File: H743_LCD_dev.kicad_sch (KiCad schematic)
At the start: 4 parts

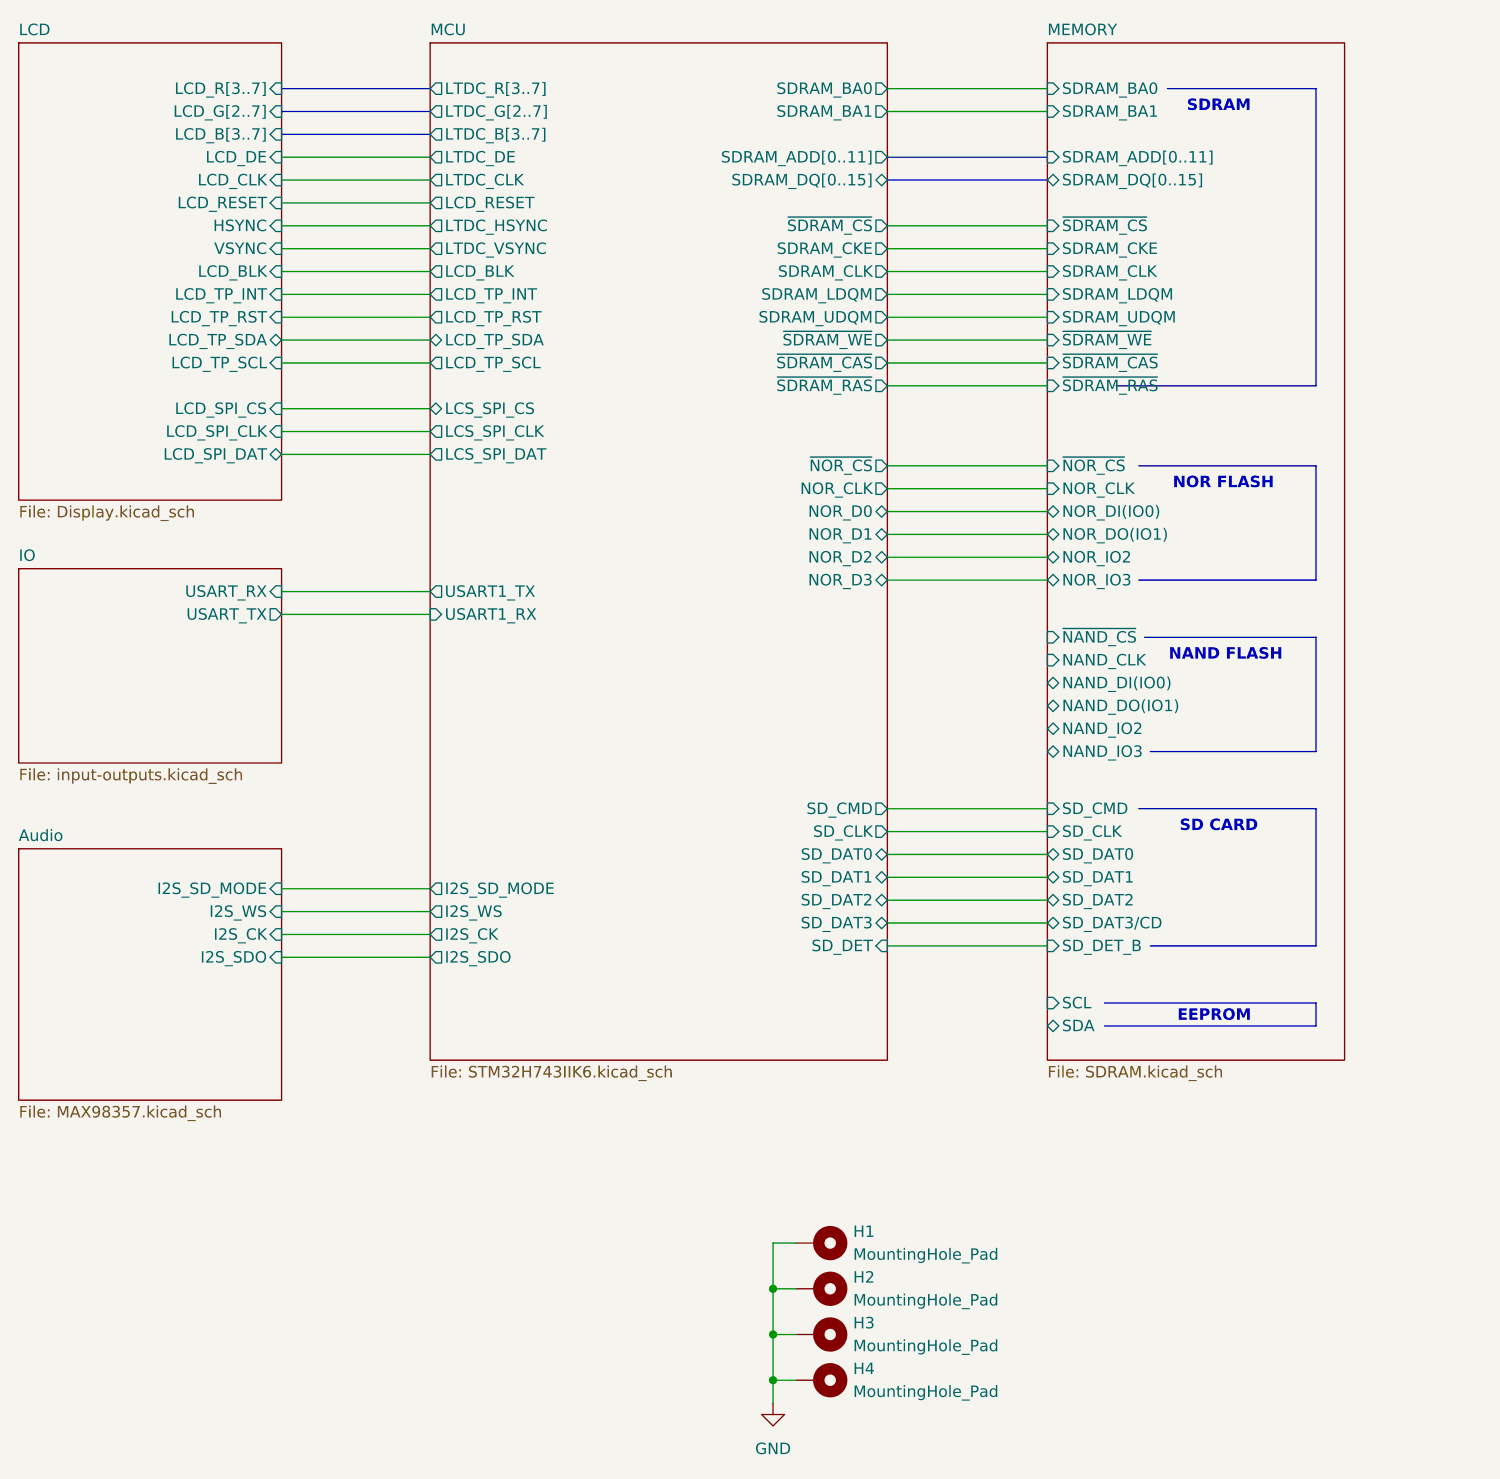
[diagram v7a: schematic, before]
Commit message: All clear (need to verify). LCD backlight driver left untracked
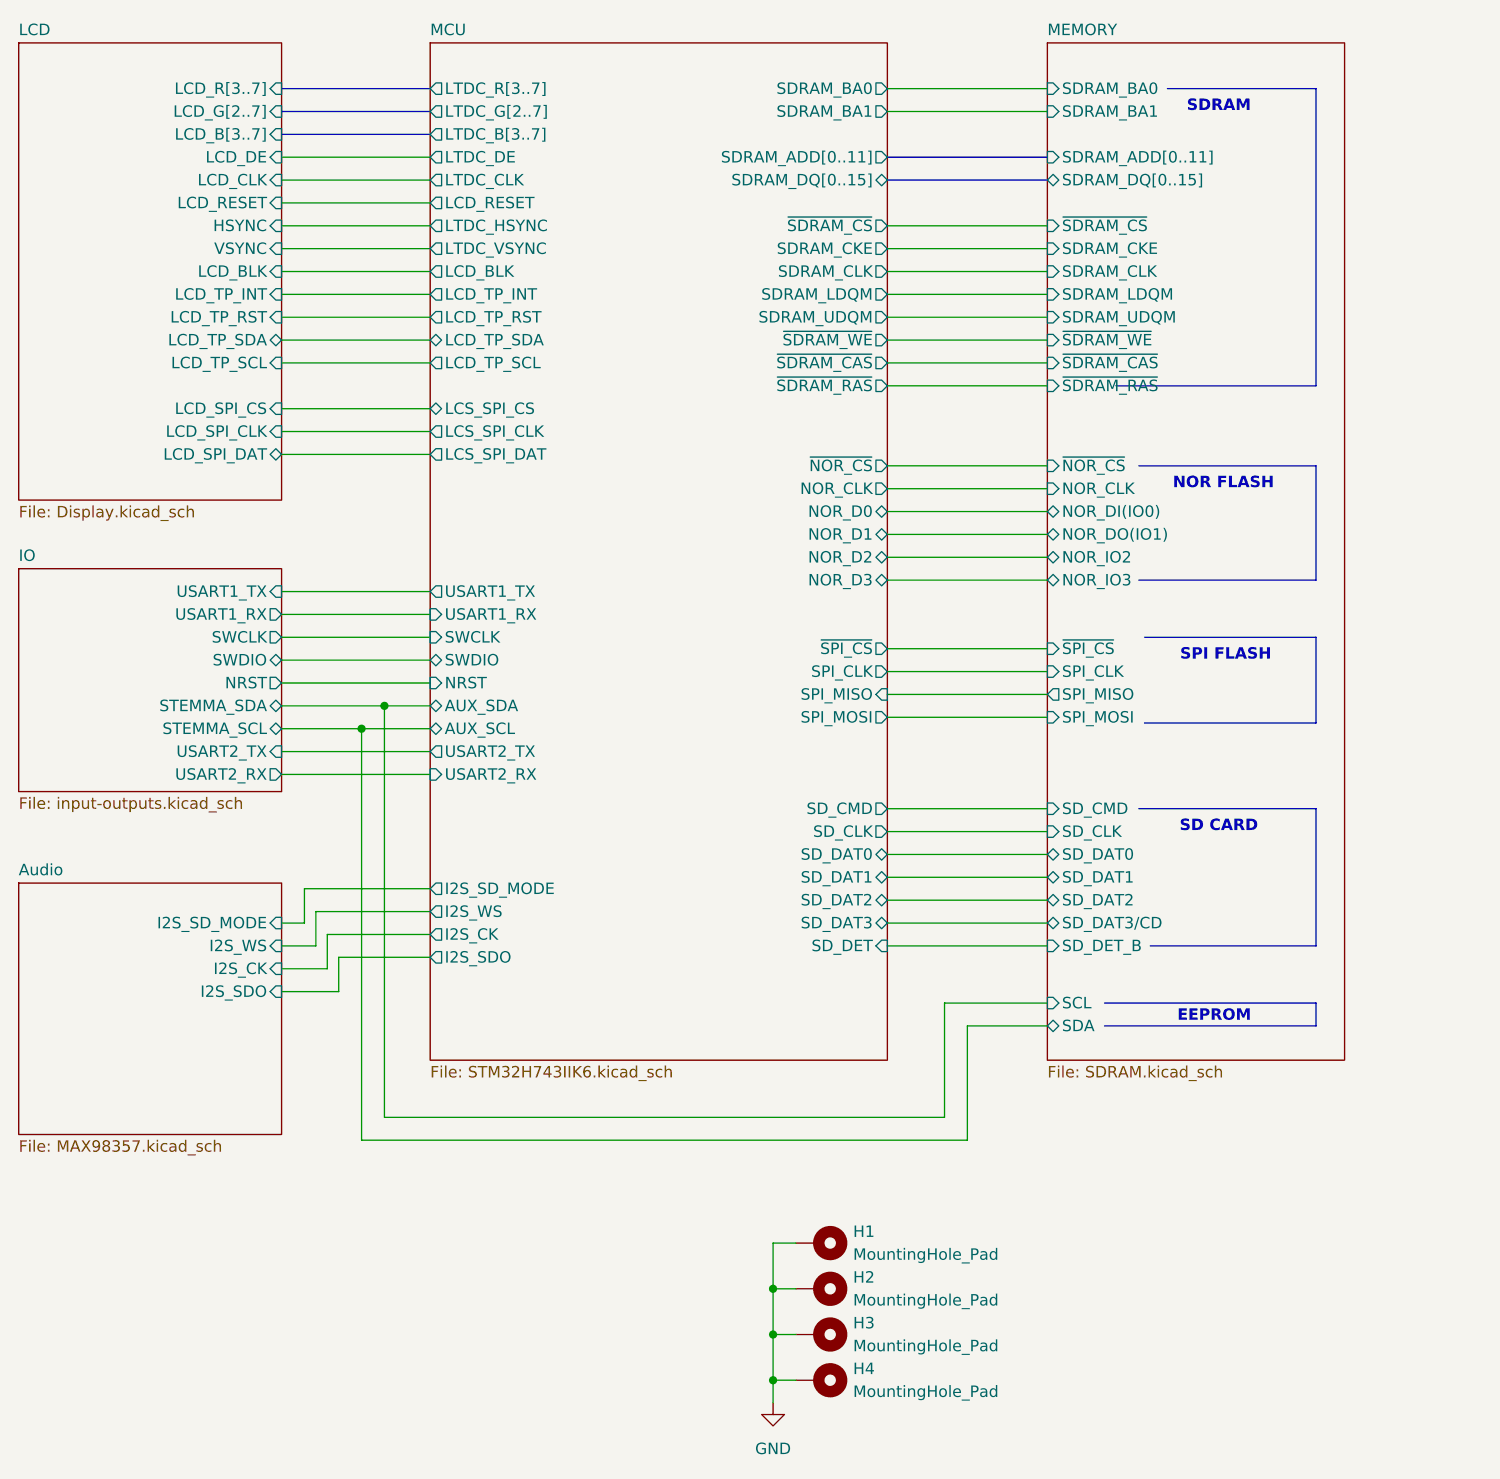
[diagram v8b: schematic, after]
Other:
- sheet IO ports: added NRST, STEMMA_SCL, STEMMA_SDA, SWCLK, SWDIO, USART1_RX, USART1_TX, USART2_RX, USART2_TX; removed USART_RX, USART_TX
- sheet MCU ports: added AUX_SCL, AUX_SDA, NRST, SPI_CLK, SPI_MISO, SPI_MOSI, SWCLK, SWDIO, USART2_RX, USART2_TX, ~{SPI_CS}; removed none
- sheet MEMORY ports: added SPI_CLK, SPI_MISO, SPI_MOSI, ~{SPI_CS}; removed NAND_CLK, NAND_DI(IO0), NAND_DO(IO1), NAND_IO2, NAND_IO3, ~{NAND_CS}
- note added: "SPI FLASH"
- note removed: "NAND FLASH"
